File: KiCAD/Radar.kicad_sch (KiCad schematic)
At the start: 19 parts, among them J1 Conn_01x15, J2 Conn_01x15, U1 LM324N_NOPB, U2 LM324N_NOPB, U3 HB100

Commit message: Layout update
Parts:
- removed J1, J2: Conn_01x15, symbol Connector_Generic:Conn_01x15
- added U4: NUCLEO-L432KC, NUCLEO-L432KC:MODULE_NUCLEO-L432KC, symbol NUCLEO-L432KC:NUCLEO-L432KC
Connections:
- net GND: now also U4.CN4_2 (GND_CN4)
- net +3.3V: now reaches U2.4
- net +3.3V: now also U1.4, U4.CN4_14 (+3V3)
- net +5V: now reaches R2.1
- net +5V: now also U3.5V, U4.CN4_4 (+5V)

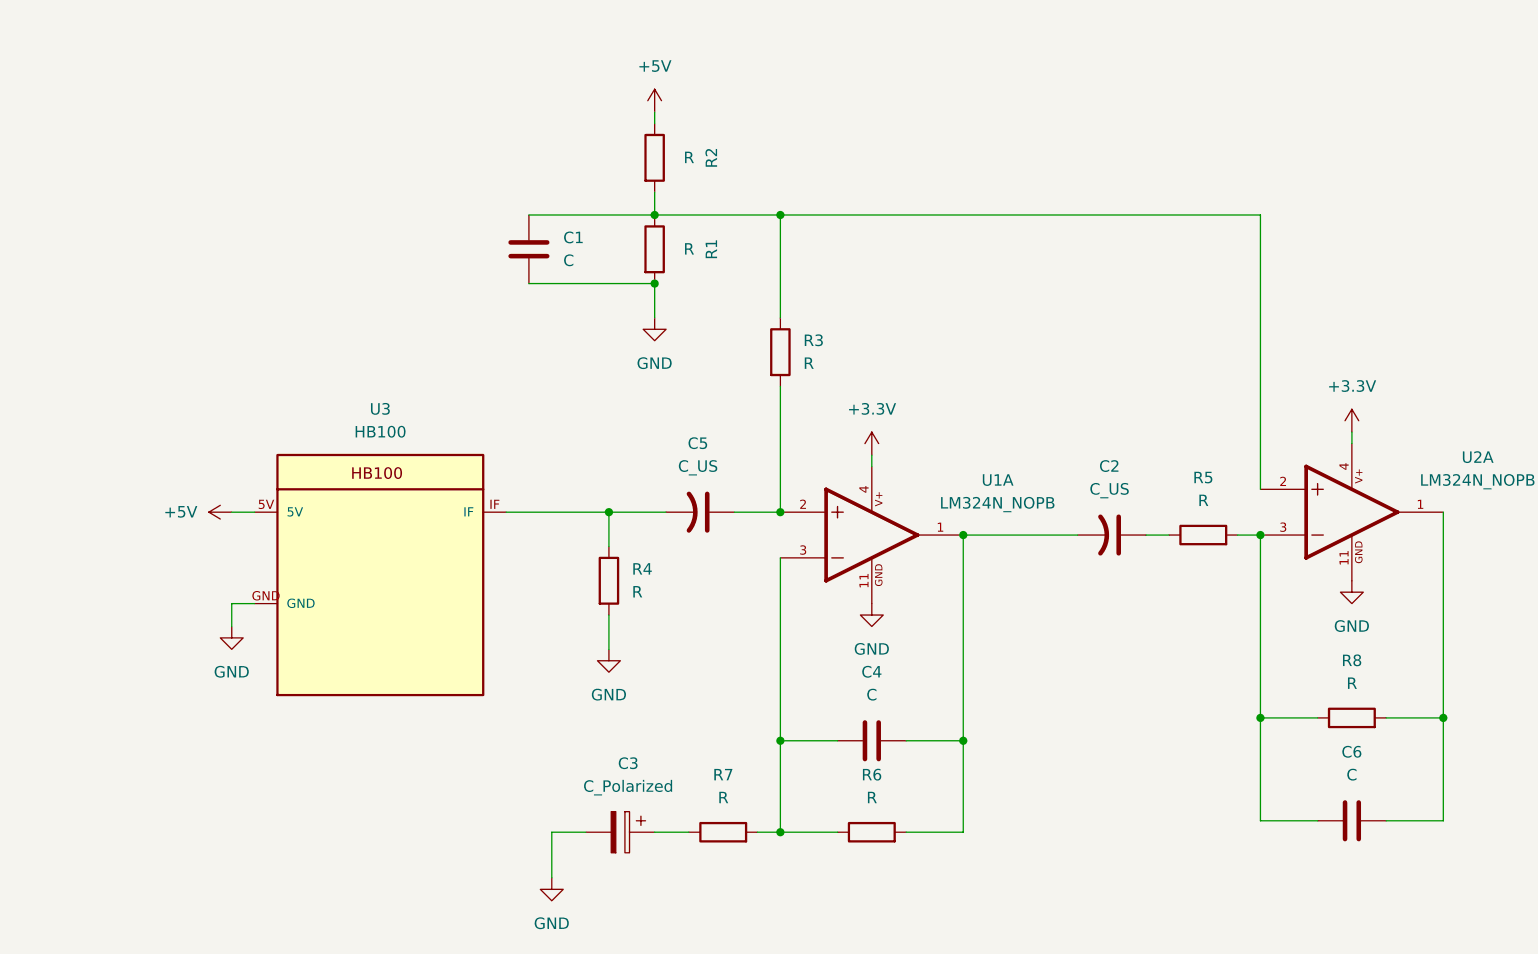
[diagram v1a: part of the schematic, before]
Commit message: added components values
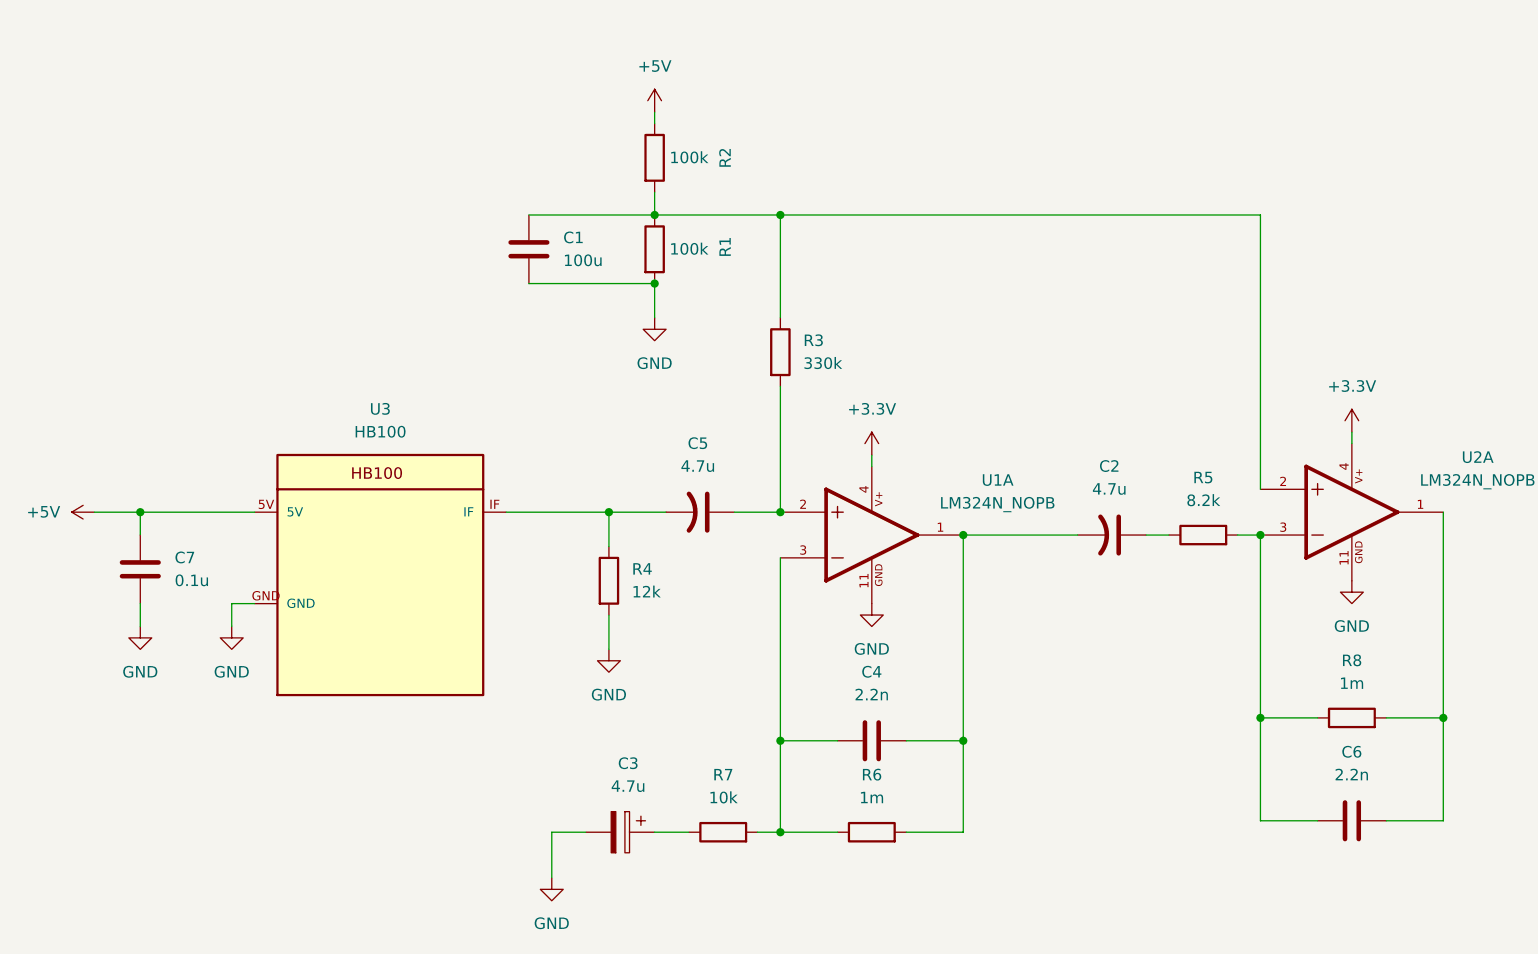
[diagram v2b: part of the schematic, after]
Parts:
- added C7: 0.1u, symbol Device:C
- C1: value C -> 100u
- C2, C5: value C_US -> 4.7u
- C3: value C_Polarized -> 4.7u
- C4, C6: value C -> 2.2n
- R1, R2: value R -> 100k
- R3: value R -> 330k
- R4: value R -> 12k
- R5: value R -> 8.2k
- R6, R8: value R -> 1m
- R7: value R -> 10k
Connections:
- net +5V: now also C7.1
- net GND: now also C7.2
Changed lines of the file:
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@@
+	)
+	(junction
+		(at 40.64 72.39)
+		(diameter 0)
+		(color 0 0 0 0)
 	)
 	(junction
@@
 	(wire
 		(pts
+			(xy 40.64 72.39) (xy 40.64 74.93)
+		)
+		(stroke
+			(width 0)
+			(type default)
+		)
+	)
+	(wire
+		(pts
 			(xy 171.45 95.25) (xy 165.1 95.25)
 		)
@@
 	(wire
 		(pts
+			(xy 40.64 72.39) (xy 53.34 72.39)
+		)
+		(stroke
+			(width 0)
+			(type default)
+		)
+	)
+	(wire
+		(pts
 			(xy 83.82 46.99) (xy 97.79 46.99)
 		)
@@
 	(wire
 		(pts
+			(xy 40.64 82.55) (xy 40.64 85.09)
+		)
+		(stroke
+			(width 0)
+			(type default)
+		)
+	)
+	(wire
+		(pts
 			(xy 97.79 107.95) (xy 101.6 107.95)
 		)
@@
 	(wire
 		(pts
-			(xy 50.8 72.39) (xy 53.34 72.39)
+			(xy 35.56 72.39) (xy 40.64 72.39)
 		)
 		(stroke
@@
 			)
 		)
-		(property "Value" "C_US"
+		(property "Value" "4.7u"
 			(at 102.616 67.31 90)
 			(effects
@@
 			)
 		)
-		(property "Value" "R"
+		(property "Value" "1m"
 			(at 121.92 104.14 90)
 			(effects
@@
 			)
 		)
-		(property "Value" "R"
+		(property "Value" "10k"
 			(at 105.41 104.14 90)
 			(effects
@@
 		(dnp no)
 		(property "Reference" "R2"
-			(at 104.14 33.02 90)
-			(effects
-				(font
-					(size 1.27 1.27)
-				)
-			)
-		)
-		(property "Value" "R"
+			(at 105.664 33.02 90)
+			(effects
+				(font
+					(size 1.27 1.27)
+				)
+			)
+		)
+		(property "Value" "100k"
 			(at 101.6 33.02 0)
 			(effects
@@
 			)
 		)
-		(property "Value" "C"
+		(property "Value" "2.2n"
 			(at 121.92 92.71 90)
 			(effects
@@
 			)
 		)
-		(property "Value" "C_Polarized"
+		(property "Value" "4.7u"
 			(at 94.869 102.87 90)
 			(effects
@@
 			)
 		)
-		(property "Value" "R"
+		(property "Value" "8.2k"
 			(at 158.75 71.12 90)
 			(effects
@@
 	)
 	(symbol
+		(lib_id "power:GND")
+		(at 40.64 85.09 0)
+		(unit 1)
+		(exclude_from_sim no)
+		(in_bom yes)
+		(on_board yes)
+		(dnp no)
+		(fields_autoplaced yes)
+		(property "Reference" "#PWR014"
+			(at 40.64 91.44 0)
+			(effects
+				(font
+					(size 1.27 1.27)
+				)
+				(hide yes)
+			)
+		)
+		(property "Value" "GND"
+			(at 40.64 90.17 0)
+			(effects
+				(font
+					(size 1.27 1.27)
+				)
+			)
+		)
+		(property "Footprint" ""
+			(at 40.64 85.09 0)
+			(effects
+				(font
+					(size 1.27 1.27)
+				)
+				(hide yes)
+			)
+		)
+		(property "Datasheet" ""
+			(at 40.64 85.09 0)
+			(effects
+				(font
+					(size 1.27 1.27)
+				)
+				(hide yes)
+			)
+		)
+		(property "Description" "Power symbol creates a global label with name \"GND\" , ground"
+			(at 40.64 85.09 0)
+			(effects
+				(font
+					(size 1.27 1.27)
+				)
+				(hide yes)
+			)
+		)
+		(pin "1"
+		)
+		(instances
+			(project ""
+				(path "/94474ebd-619e-4dae-8df3-623d385c4187"
+					(reference "#PWR014")
+					(unit 1)
+				)
+			)
+		)
+	)
+	(symbol
 		(lib_id "Device:R")
 		(at 175.26 95.25 90)
@@
 			)
 		)
-		(property "Value" "R"
+		(property "Value" "1m"
 			(at 175.26 91.44 90)
 			(effects
@@
 		(dnp no)
 		(property "Reference" "R1"
-			(at 104.14 43.18 90)
-			(effects
-				(font
-					(size 1.27 1.27)
-				)
-			)
-		)
-		(property "Value" "R"
+			(at 105.664 42.926 90)
+			(effects
+				(font
+					(size 1.27 1.27)
+				)
+			)
+		)
+		(property "Value" "100k"
 			(at 101.6 43.18 0)
 			(effects
@@
 			)
 		)
-		(property "Value" "R"
+		(property "Value" "12k"
 			(at 95.25 81.2799 0)
 			(effects
@@
 			)
 		)
-		(property "Value" "C_US"
+		(property "Value" "4.7u"
 			(at 148.336 69.85 90)
 			(effects
@@
 	(symbol
 		(lib_id "power:+5V")
-		(at 50.8 72.39 90)
+		(at 35.56 72.39 90)
 		(unit 1)
 		(exclude_from_sim no)
@@
 		(fields_autoplaced yes)
 		(property "Reference" "#PWR013"
-			(at 54.61 72.39 0)
+			(at 39.37 72.39 0)
 			(effects
 				(font
@@
 		)
 		(property "Value" "+5V"
-			(at 46.99 72.3899 90)
+			(at 31.75 72.3899 90)
 			(effects
 				(font
@@
 		)
 		(property "Footprint" ""
-			(at 50.8 72.39 0)
+			(at 35.56 72.39 0)
 			(effects
 				(font
@@
 		)
 		(property "Datasheet" ""
-			(at 50.8 72.39 0)
+			(at 35.56 72.39 0)
 			(effects
 				(font
@@
 		)
 		(property "Description" "Power symbol creates a global label with name \"+5V\""
-			(at 50.8 72.39 0)
+			(at 35.56 72.39 0)
 			(effects
 				(font
@@
 			)
 		)
-		(property "Value" "C"
+		(property "Value" "2.2n"
 			(at 175.26 101.6 90)
 			(effects
@@
 	)
 	(symbol
+		(lib_id "Device:C")
+		(at 40.64 78.74 0)
+		(unit 1)
+		(exclude_from_sim no)
+		(in_bom yes)
+		(on_board yes)
+		(dnp no)
+		(fields_autoplaced yes)
+		(property "Reference" "C7"
+			(at 44.45 77.4699 0)
+			(effects
+				(font
+					(size 1.27 1.27)
+				)
+				(justify left)
+			)
+		)
+		(property "Value" "0.1u"
+			(at 44.45 80.0099 0)
+			(effects
+				(font
+					(size 1.27 1.27)
+				)
+				(justify left)
+			)
+		)
+		(property "Footprint" ""
+			(at 41.6052 82.55 0)
+			(effects
+				(font
+					(size 1.27 1.27)
+				)
+				(hide yes)
+			)
+		)
+		(property "Datasheet" "~"
+			(at 40.64 78.74 0)
+			(effects
+				(font
+					(size 1.27 1.27)
+				)
+				(hide yes)
+			)
+		)
+		(property "Description" "Unpolarized capacitor"
+			(at 40.64 78.74 0)
+			(effects
+				(font
+					(size 1.27 1.27)
+				)
+				(hide yes)
+			)
+		)
+		(pin "1"
+		)
+		(pin "2"
+		)
+		(instances
+			(project ""
+				(path "/94474ebd-619e-4dae-8df3-623d385c4187"
+					(reference "C7")
+					(unit 1)
+				)
+			)
+		)
+	)
+	(symbol
 		(lib_id "power:GND")
 		(at 92.71 87.63 0)
@@
 			)
 		)
-		(property "Value" "R"
+		(property "Value" "330k"
 			(at 114.3 55.8799 0)
 			(effects
@@
 			)
 		)
-		(property "Value" "C"
+		(property "Value" "100u"
 			(at 87.63 44.4499 0)
 			(effects

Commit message: Layout V1
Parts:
- removed C2, C5: 4.7u, symbol Device:C_US
- added C2, C5: 4.7u, Capacitor_SMD:CP_Elec_4x5.4, symbol Device:C_Polarized
- C1, C4, C6, C7: footprint (none) -> Capacitor_SMD:C_0603_1608Metric_Pad1.08x0.95mm_HandSolder
- C3: footprint (none) -> Capacitor_SMD:CP_Elec_4x5.4
- R1, R2, R3, R4, R5, R6, R7, R8: footprint (none) -> Resistor_SMD:R_0603_1608Metric_Pad0.98x0.95mm_HandSolder
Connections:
- net at R3.2, U1.2: now also C2.1
- net at R4.1, U3.IF: now also C2.2
- net at C4.2, R6.2, U1.1: now also C5.2
- net at C6.2, R8.2, U2.1: now also U4.CN4_10 (PA3)
- net at R5.1: now also C5.1
- no-connect marks 0 -> 26
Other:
- moved on the sheet: C1, C4, C6, C7, R1, R2, R3, R4, R5, R6, R7, R8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

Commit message: Layout V2
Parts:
- removed U1, U2: LM324N_NOPB, LM324N_NOPB:DIP825W47P254L1917H533Q14, symbol LM324:LM324N_NOPB
- added U5: LM358DR, D8, symbol Radar:LM358DR
- U3: footprint HB100:HB100 -> Footprinty:HB100
- U4: footprint NUCLEO-L432KC:MODULE_NUCLEO-L432KC -> Footprinty:MODULE_NUCLEO-L432KC
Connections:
- net +3.3V: now also U5.8 (VCC)
- net GND: now also U5.4 (GND)
- net at C4.1, R6.1, R7.2: now also U5.2 (1IN-)
- net at C4.2, C5.2, R6.2: now also U5.1 (1OUT)
- net 2OUT: now reaches C6.2, R8.2, U4.CN4_10 (PA3)
- net 2OUT: now also U5.7 (2OUT)
- net 2IN+: now reaches C1.1, R1.1, R2.2, R3.1
- net 2IN+: now also U5.5 (2IN+)
- net 2IN-: now reaches C6.1, R5.2, R8.1
- net 2IN-: now also U5.6 (2IN-)
- net 1IN+: now reaches C2.1, R3.2
- net 1IN+: now also U5.3 (1IN+)
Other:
- moved on the sheet: C1, C2, C3, C4, C5, C6, C7, R1, R2, R3, R4, R5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
